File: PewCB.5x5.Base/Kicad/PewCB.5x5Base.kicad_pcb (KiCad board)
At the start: 2 copper layers, 83.8 x 83.8 mm, 4 parts

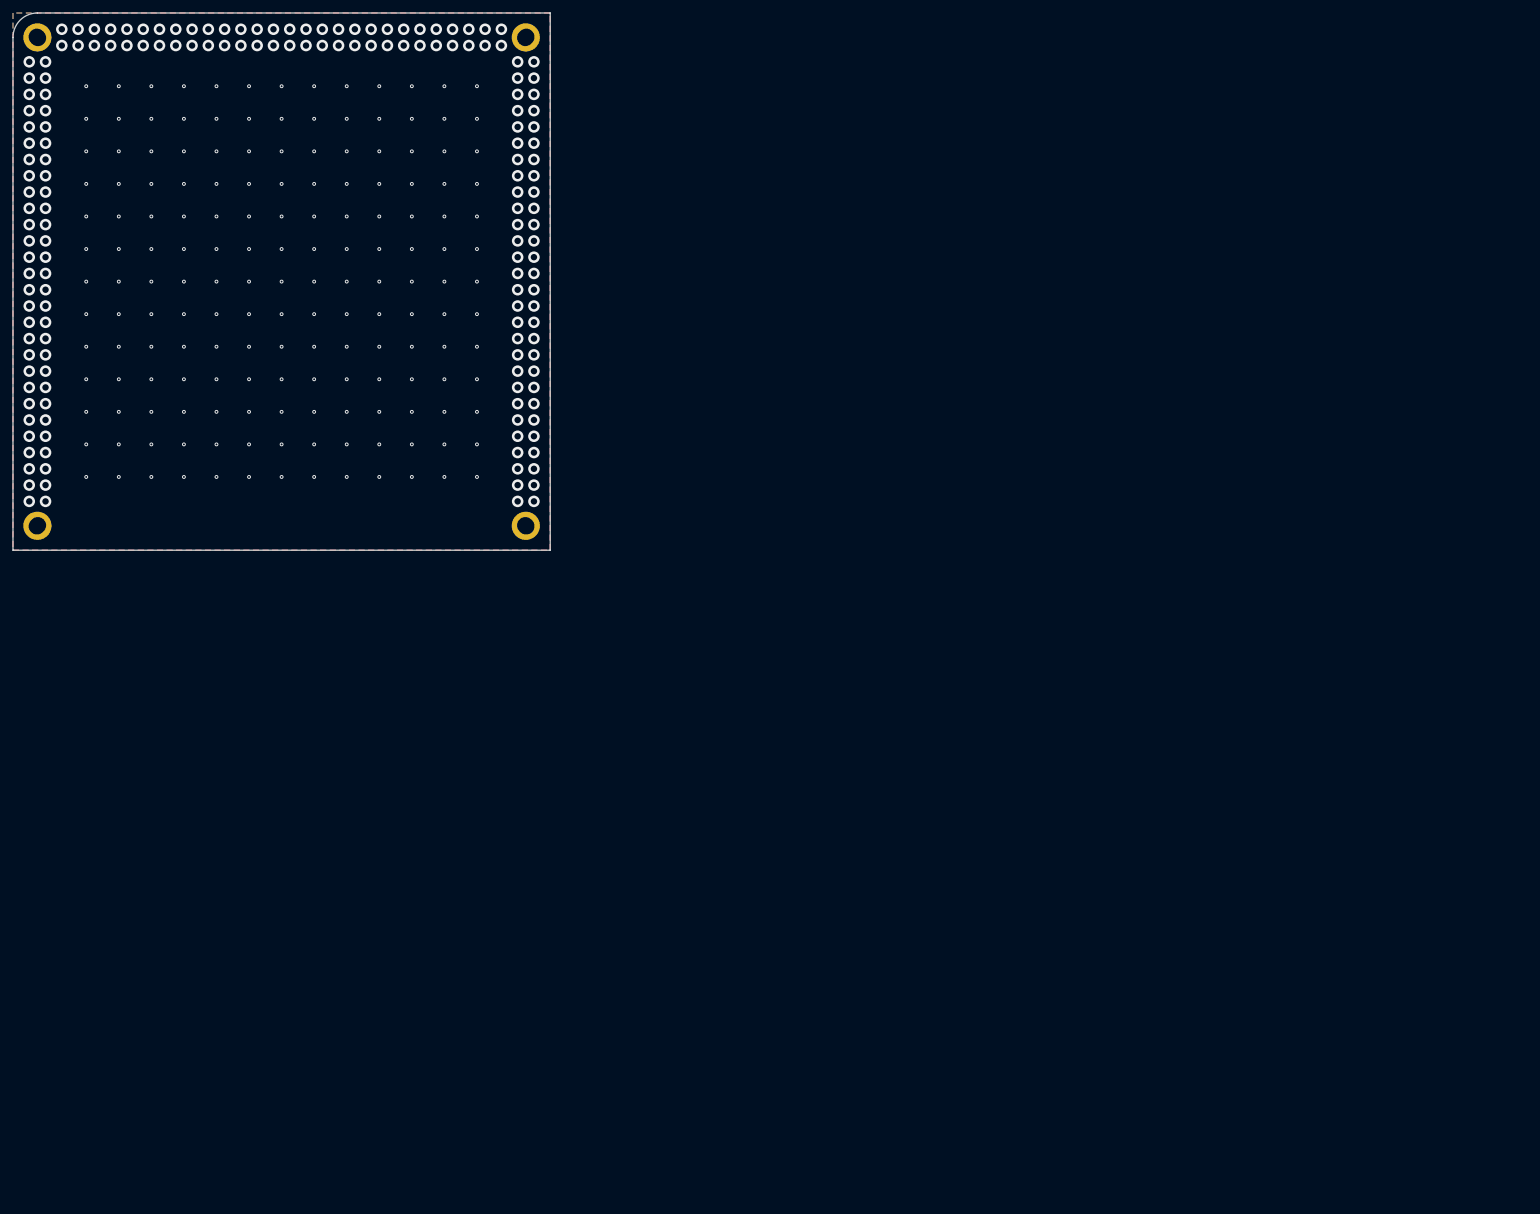
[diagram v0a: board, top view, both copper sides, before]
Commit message: fixed kicad board origins
removed empty page layouts
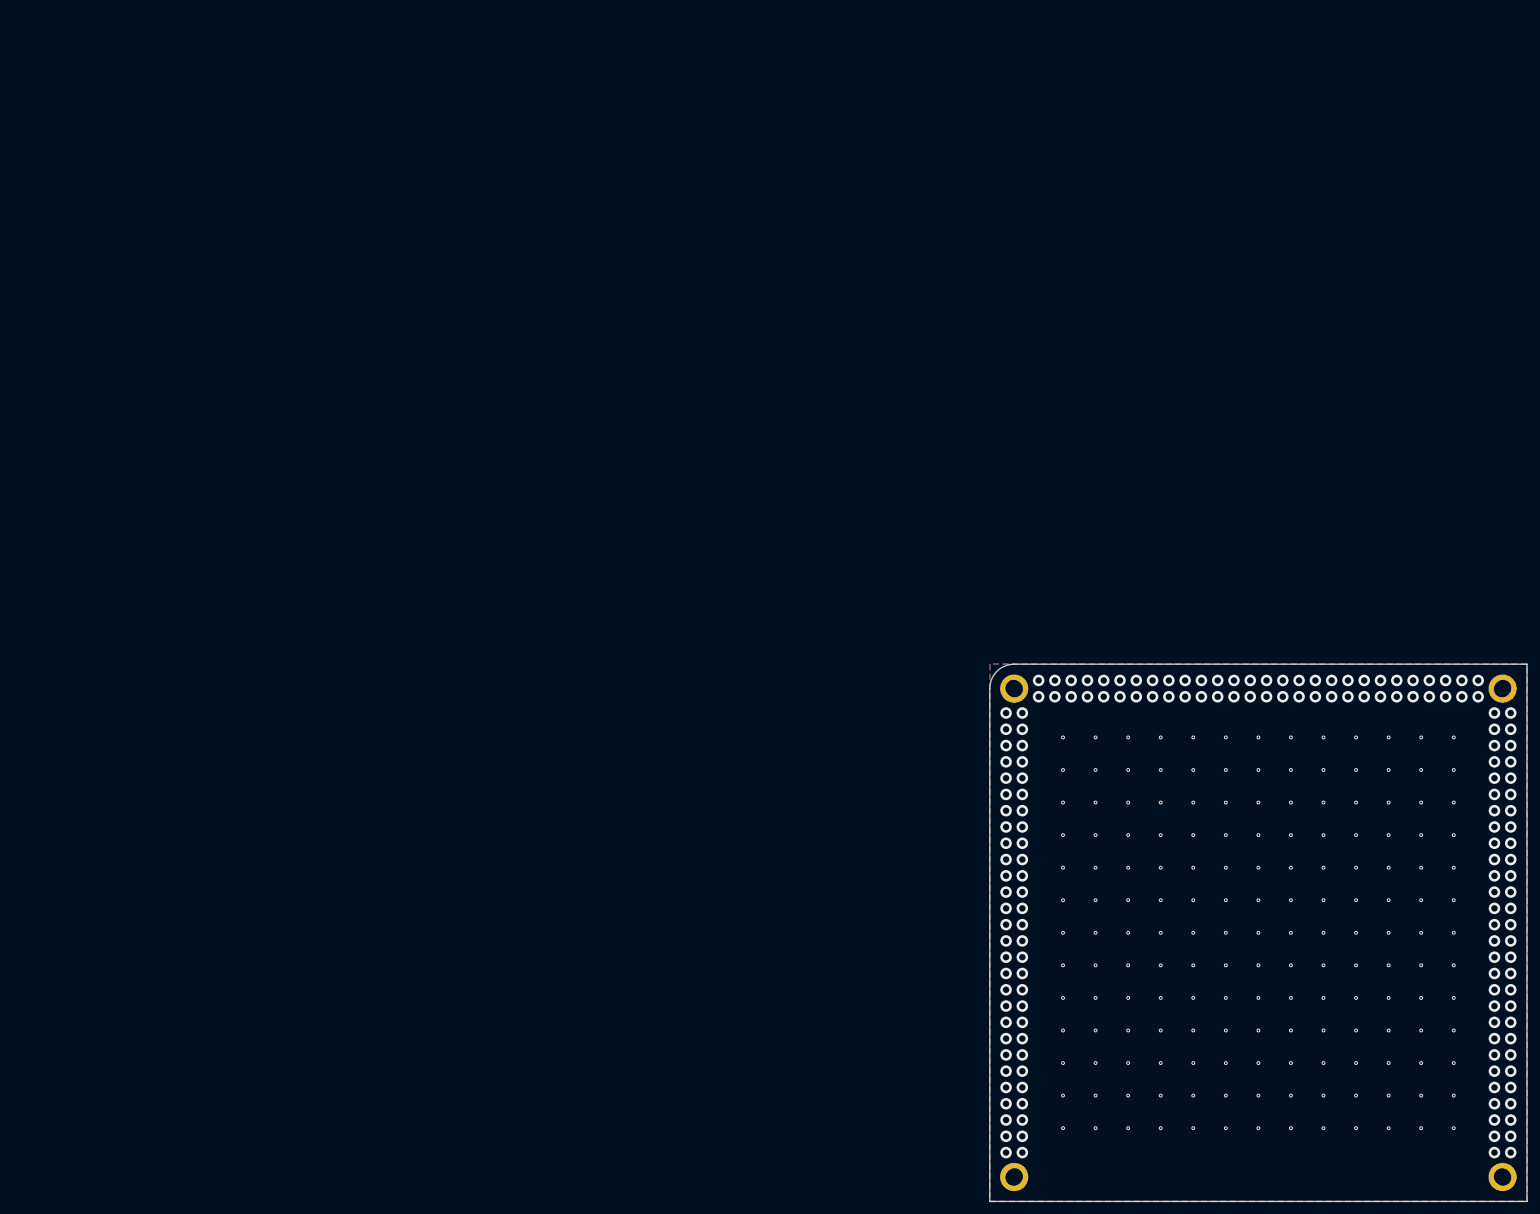
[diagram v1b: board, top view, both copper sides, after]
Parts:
- moved H** 183.2 mm to (114.3, 63.5)
- moved H** 183.2 mm to (190.5, 139.7)
- moved H** 183.2 mm to (190.5, 63.5)
- moved H** 183.2 mm to (114.3, 139.7)
